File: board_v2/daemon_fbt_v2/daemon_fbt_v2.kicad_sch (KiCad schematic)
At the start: 58 parts, among them IC1 NPM1100-QDAA-R7, IC2 nRF52840-QFAA-F-R7, IC3 MX25R6435FZAIL0-TR, J1 P70-5100045, J2 P70-5100045, J3 150mAh, Q1 FDV303N, U1 BMM350, U2 BHI360, Y1 ECS-320-8-37B2-CTN-TR

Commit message: update flash memory from 64Mbit to 2Mbit and create footprint
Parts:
- IC3: value MX25R6435FZAIL0-TR -> MX25U2035FZUI-TR; footprint the_backrooms:SON80P400X400X60-9N -> the_backrooms:SON50P200X300X60-9N; Manufacturer_Part_Number MX25R6435FZAIL0-TR -> MX25U2035FZUI-TR; Mfr. No. MX25R6435FZAIL0-TR -> MX25U2035FZUI-TR; Mouser Part Number 95-25R6435FZAIL0TR -> MX25U2035FZUI-TR; Mouser Price/Stock https://www.mouser.co.uk/ProductDetail/Macronix/MX25R6435FZ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 -> (none)
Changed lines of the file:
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@@
       (effects (font (size 1.27 1.27)))
     )
-    (property "Value" "MX25R6435FZAIL0-TR" (at 75.565 140.335 0)
+    (property "Value" "MX25U2035FZUI-TR" (at 75.565 140.335 0)
       (effects (font (size 1.27 1.27)))
     )
-    (property "Footprint" "the_backrooms:SON80P400X400X60-9N" (at 86.995 218.745 0)
+    (property "Footprint" "the_backrooms:SON50P200X300X60-9N" (at 86.995 218.745 0)
       (effects (font (size 1.27 1.27)) (justify left top) hide)
     )
-    (property "Datasheet" "https://www.mouser.com/datasheet/2/819/MX25R6435F_2c_Wide_Range_2c_64Mb_2c_v1_6-3370962.pdf" (at 86.995 318.745 0)
+    (property "Datasheet" "https://www.mouser.de/datasheet/2/819/MX25U2035F_2c_1_8V_2c_2Mb_2c_v1_1-3371144.pdf" (at 86.995 318.745 0)
       (effects (font (size 1.27 1.27)) (justify left top) hide)
     )
@@
       (effects (font (size 1.27 1.27)) (justify left top) hide)
     )
-    (property "Manufacturer_Part_Number" "MX25R6435FZAIL0-TR" (at 86.995 718.745 0)
+    (property "Manufacturer_Part_Number" "MX25U2035FZUI-TR" (at 86.995 718.745 0)
       (effects (font (size 1.27 1.27)) (justify left top) hide)
     )
-    (property "Mouser Part Number" "95-25R6435FZAIL0TR" (at 86.995 818.745 0)
+    (property "Mouser Part Number" "MX25U2035FZUI-TR" (at 86.995 818.745 0)
       (effects (font (size 1.27 1.27)) (justify left top) hide)
     )
-    (property "Mouser Price/Stock" "https://www.mouser.co.uk/ProductDetail/Macronix/MX25R6435FZAIL0-TR?qs=mELouGlnn3cK%252BXKdc9RzBg%3D%3D" (at 86.995 918.745 0)
+    (property "Mouser Price/Stock" "" (at 86.995 918.745 0)
       (effects (font (size 1.27 1.27)) (justify left top) hide)
     )
@@
       (effects (font (size 1.27 1.27)) (justify left top) hide)
     )
-    (property "Mfr. No." "MX25R6435FZAIL0-TR" (at 29.845 123.825 0)
+    (property "Mfr. No." "MX25U2035FZUI-TR" (at 29.845 123.825 0)
       (effects (font (size 1.27 1.27)) hide)
     )
+    (property "Package/Case" "" (at 29.845 123.825 0)
+      (effects (font (size 1.27 1.27)) hide)
+    )
+    (property "Description" "" (at 29.845 123.825 0)
+      (effects (font (size 1.27 1.27)) hide)
+    )

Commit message: added more mfr. no. into the data fields
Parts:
- IC1: Mfr. No. (none) -> NPM1100-QDAA-R7
- Q1: Mfr. No. (none) -> FDV303N
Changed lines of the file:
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@@
       (effects (font (size 1.27 1.27)) (justify left top) hide)
+    )
+    (property "Mfr. No." "FDV303N" (at 260.35 140.97 0)
+      (effects (font (size 1.27 1.27)) hide)
+    )
+    (property "Package/Case" "" (at 260.35 140.97 0)
+      (effects (font (size 1.27 1.27)) hide)
+    )
+    (property "Description" "" (at 260.35 140.97 0)
+      (effects (font (size 1.27 1.27)) hide)
     )
     (pin "1")
@@
       (effects (font (size 1.27 1.27)) (justify left top) hide)
     )
+    (property "Mfr. No." "NPM1100-QDAA-R7" (at 40.005 57.15 0)
+      (effects (font (size 1.27 1.27)))
+    )
+    (property "Package/Case" "" (at 40.005 57.15 0)
+      (effects (font (size 1.27 1.27)) hide)
+    )
+    (property "Description" "" (at 40.005 57.15 0)
+      (effects (font (size 1.27 1.27)) hide)
+    )
     (pin "22")

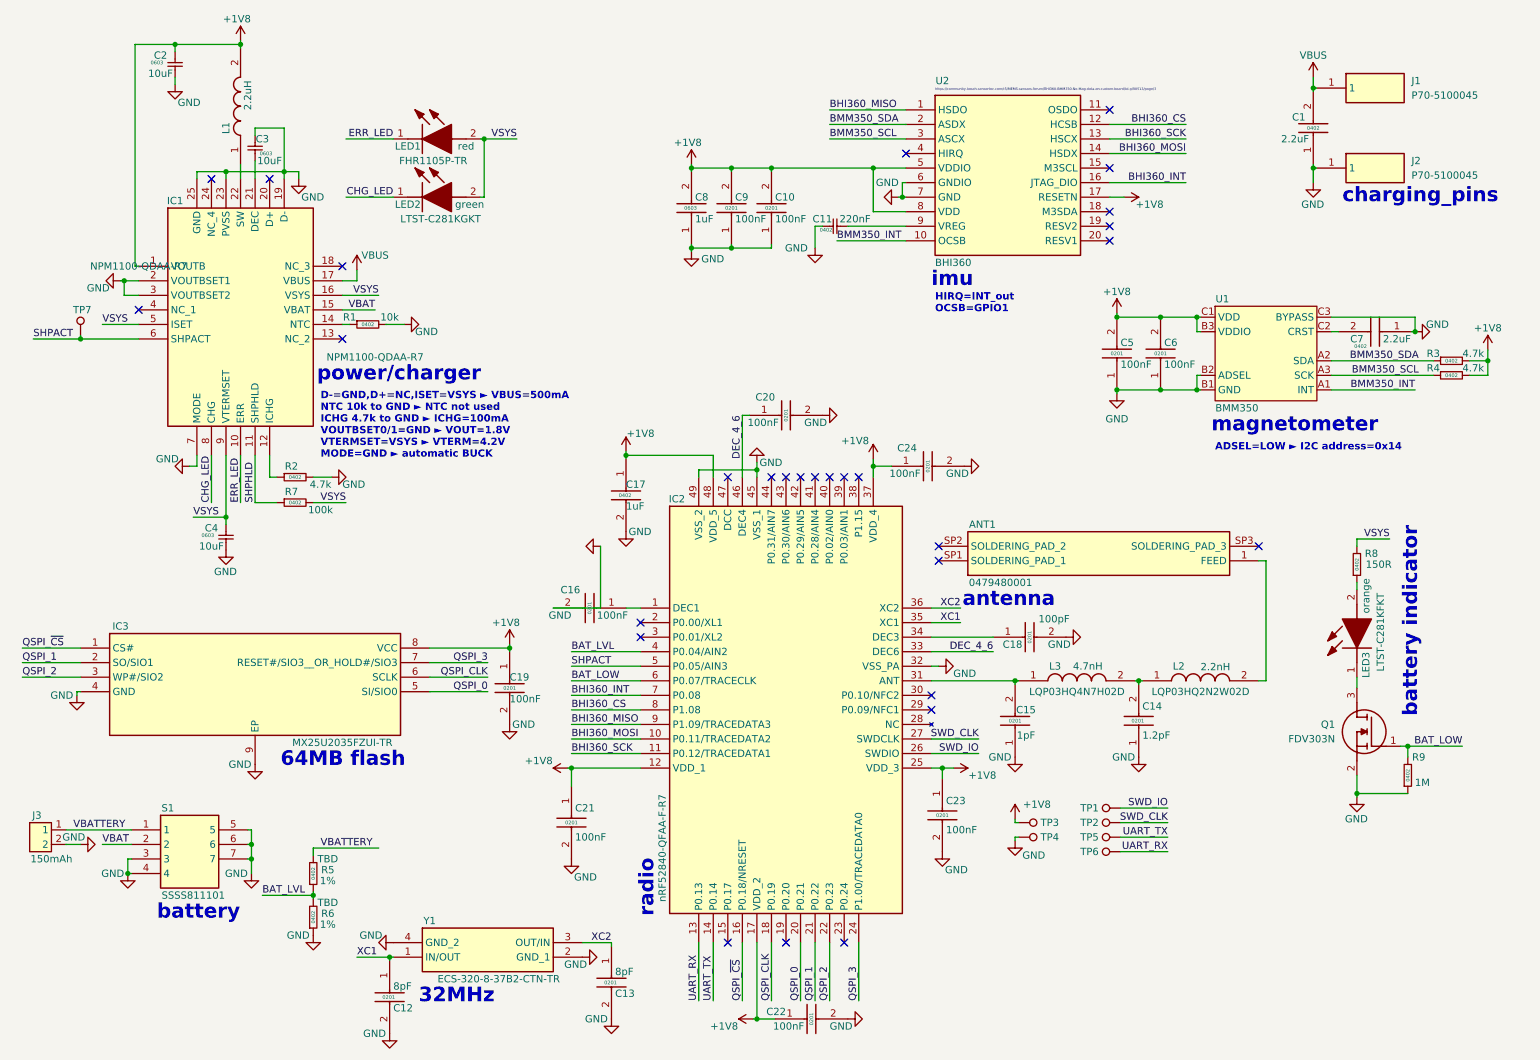
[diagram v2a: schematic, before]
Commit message: reduce price of some components
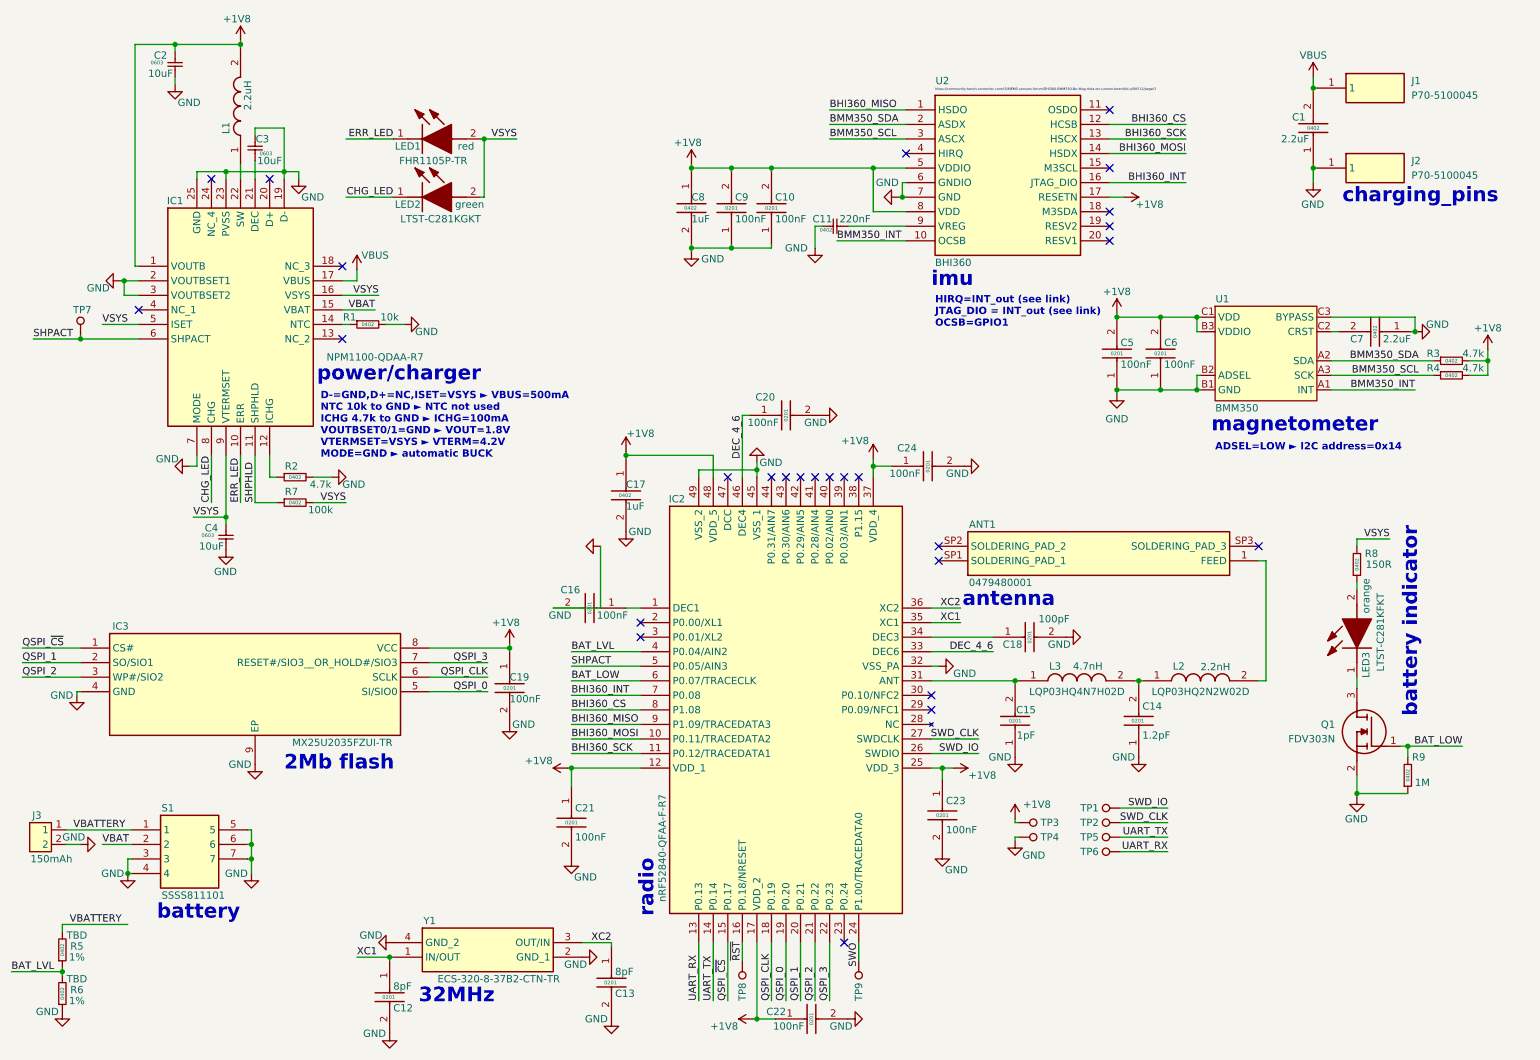
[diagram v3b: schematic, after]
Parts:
- removed C8: 1uF, the_backrooms:CAPC1608X90N, symbol the_backrooms:0603ZD105JAT2A
- added C8: 1uF, the_backrooms:CAPC1005X55N, symbol the_backrooms:GRM155C71C105KE11J
- added TP8, TP9: ~, the_backrooms:tp_1mm, symbol the_backrooms:tp_1mm
- C1, C7: Arrow Part Number GRM155R61E225KE11D -> (none); Arrow Price/Stock https://www.arrow.com/en/products/grm155r61e225ke11d/murata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 -> (none); Manufacturer_Part_Number GRM155R61E225KE11D -> GRM155R61A225KE01J; Mfr. No. GRM155R61E225KE11D -> GRM155R61A225KE01J; Mouser Part Number 81-GRM155R61E225KE1D -> 81-GRM155R61A225K01J; Mouser Price/Stock https://www.mouser.co.uk/ProductDetail/Murata-Electronics/G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 -> (none)
- C2, C3, C4: Mfr. No. GRM188R60J106KE47D -> GRM188R60J106KE47J
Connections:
- net +1V8: now also C8.1
- net GND: now also C8.2
- net QSPI_0: now also IC2.19 (P0.20); no longer IC2.20 (P0.21)
- net QSPI_1: now also IC2.20 (P0.21); no longer IC2.21 (P0.22)
- net QSPI_2: now also IC2.21 (P0.22); no longer IC2.22 (P0.23)
- net QSPI_3: now also IC2.22 (P0.23); no longer IC2.24 (P1.00/TRACEDATA0)
- net QSPI_~{CS}: now also IC2.15 (P0.17); no longer IC2.16 (P0.18/NRESET)
- new net SWO: IC2.24 (P1.00/TRACEDATA0), TP9.1
- new net ~{RST}: IC2.16 (P0.18/NRESET), TP8.1
- no-connect marks 29 -> 27
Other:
- note added: "2Mb flash"
- note added: "HIRQ=INT_out (see link) JTAG_DIO = INT_out (see link) OCSB=GPIO1"
- note removed: "64MB flash"
- note removed: "HIRQ=INT_out OCSB=GPIO1"
- moved on the sheet: R5, R6

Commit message: finished redesign; lets hope jlcpcb doesn't kill me
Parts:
- removed S1: SSSS811101, SSSS811101, symbol the_backrooms:SSSS811101
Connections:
- net VBATTERY is gone; now on net VBAT: J3.1, R5.2
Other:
- moved on the sheet: J3, R5, R6
